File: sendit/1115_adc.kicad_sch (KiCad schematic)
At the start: 5 parts, among them U7 ADS1115IDGSR

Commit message: more work towards rev c board.
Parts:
- removed R19, R20: 2.2k, Resistor_SMD:R_0603_1608Metric, symbol Device:R_Small_US
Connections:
- net +3.3V renamed +3.3VADC
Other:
- moved on the sheet: C20, C21

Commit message: big change removing the usb hub and serial chip.
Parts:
- renumbered C20 to C12, C21 to C13, U7 to U5
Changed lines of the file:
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@@
 		(on_board yes)
 		(dnp no)
-		(property "Reference" "C20"
+		(property "Reference" "C12"
 			(at 160.02 80.0163 0)
 			(effects
@@
 			(project "sendit"
 				(path "/a355e4d0-2918-44fc-be8d-2503b84c6d6c/8455ca3a-09fb-49d0-8692-dd30220f1ed8"
-					(reference "C23")
+					(reference "C15")
 					(unit 1)
 				)
 				(path "/a355e4d0-2918-44fc-be8d-2503b84c6d6c/8b22d84f-0b54-48cc-b723-35a0934e8e0a"
-					(reference "C20")
+					(reference "C12")
 					(unit 1)
 				)
@@
 		(on_board yes)
 		(dnp no)
-		(property "Reference" "C21"
+		(property "Reference" "C13"
 			(at 171.45 80.0163 0)
 			(effects
@@
 			(project "sendit"
 				(path "/a355e4d0-2918-44fc-be8d-2503b84c6d6c/8455ca3a-09fb-49d0-8692-dd30220f1ed8"
-					(reference "C24")
+					(reference "C16")
 					(unit 1)
 				)
 				(path "/a355e4d0-2918-44fc-be8d-2503b84c6d6c/8b22d84f-0b54-48cc-b723-35a0934e8e0a"
-					(reference "C21")
+					(reference "C13")
 					(unit 1)
 				)
@@
 		(on_board yes)
 		(dnp no)
-		(property "Reference" "#PWR025"
+		(property "Reference" "#PWR027"
 			(at 123.19 67.31 0)
 			(effects
@@
 			(project "sendit"
 				(path "/a355e4d0-2918-44fc-be8d-2503b84c6d6c/8455ca3a-09fb-49d0-8692-dd30220f1ed8"
-					(reference "#PWR040")
+					(reference "#PWR042")
 					(unit 1)
 				)
 				(path "/a355e4d0-2918-44fc-be8d-2503b84c6d6c/8b22d84f-0b54-48cc-b723-35a0934e8e0a"
-					(reference "#PWR025")
+					(reference "#PWR027")
 					(unit 1)
 				)
@@
 		(dnp no)
 		(fields_autoplaced yes)
-		(property "Reference" "U7"
+		(property "Reference" "U5"
 			(at 129.1941 71.12 0)
 			(effects
@@
 			(project "sendit"
 				(path "/a355e4d0-2918-44fc-be8d-2503b84c6d6c/8455ca3a-09fb-49d0-8692-dd30220f1ed8"
-					(reference "U8")
+					(reference "U6")
 					(unit 1)
 				)
 				(path "/a355e4d0-2918-44fc-be8d-2503b84c6d6c/8b22d84f-0b54-48cc-b723-35a0934e8e0a"
-					(reference "U7")
+					(reference "U5")
 					(unit 1)
 				)
@@
 		(dnp no)
 		(fields_autoplaced yes)
-		(property "Reference" "#PWR026"
+		(property "Reference" "#PWR028"
 			(at 127 105.41 0)
 			(effects
@@
 			(project "sendit"
 				(path "/a355e4d0-2918-44fc-be8d-2503b84c6d6c/8455ca3a-09fb-49d0-8692-dd30220f1ed8"
-					(reference "#PWR041")
+					(reference "#PWR043")
 					(unit 1)
 				)
 				(path "/a355e4d0-2918-44fc-be8d-2503b84c6d6c/8b22d84f-0b54-48cc-b723-35a0934e8e0a"
-					(reference "#PWR026")
-					(unit 1)
-				)
+					(reference "#PWR028")
+					(unit 1)
+				)

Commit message: fixed erc errors
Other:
- moved on the sheet: C12, C13, U5

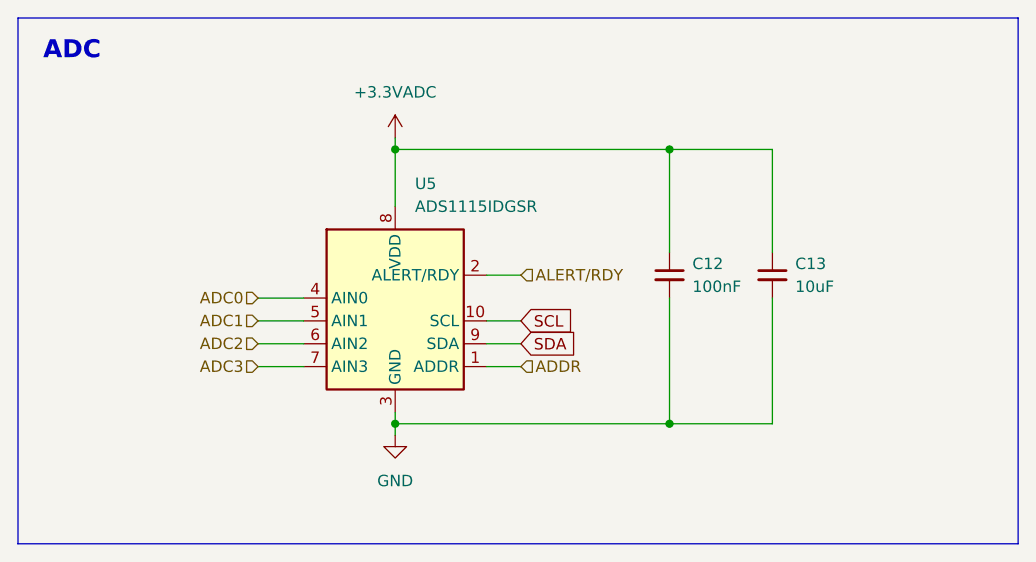
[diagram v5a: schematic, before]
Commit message: added pullup resistors to ads1115 alert line
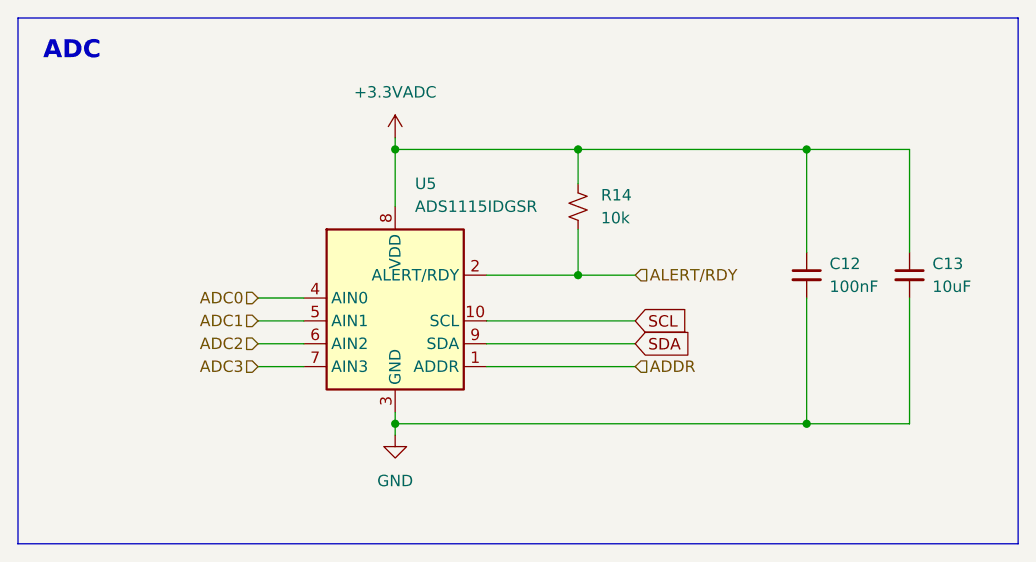
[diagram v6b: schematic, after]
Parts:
- added R14: 10k, Resistor_SMD:R_0603_1608Metric, symbol Device:R_Small_US
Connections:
- net +3.3VADC: now also R14.1
- net ALERT/RDY: now also R14.2
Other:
- moved on the sheet: C12, C13
